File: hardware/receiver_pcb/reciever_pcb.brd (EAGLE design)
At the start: 54 x 27 mm, 26 parts

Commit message: better dir struct, and some tweaks to pcbs
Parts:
- removed R6: 220, rcl:R0805
- removed T1: (no value), transistor:SOT23-BCE
- added LED2: (no value), led:CHIP-LED0805
- R4, R5: value 10K -> 470
- moved R5 10.4 mm to (32.4, 21.9), turned to 90 degrees
- moved TP2 10.1 mm to (36.1, 18.6)
- moved R4 9.09 mm to (30.0, 22.0), turned to 90 degrees
- moved LED1 2.26 mm to (32.4, 18.1), turned to 180 degrees
- moved X1 1.00 mm to (43.8, 23.0)
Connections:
- removed net N$12: R6.2, T1.C, X3.3
- new net N$13: LED2.C, TP1.TP, U$1.P$15
- net +4.1V: now also R4.2, R5.2; no longer T1.E
- net GND: no longer LED1.C
- net N$10: now also LED2.A; no longer TP1.TP, U$1.P$15
- net N$11: now also R5.1; no longer R6.1
- net N$9: now also LED1.C; no longer R5.1, T1.B
- net VCC: no longer R4.2, R5.2
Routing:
- net +4.1V: track 40.7 -> 78.3 mm
- net N$9: track 33.3 -> 8.84 mm
- net N$12: track 14.0 -> 0.00 mm, vias 1 -> 0
- net GND: track 42.8 -> 30.7 mm, vias 2 -> 0
- net N$10: track 12.9 -> 2.00 mm
- net N$13: track 0.00 -> 8.68 mm
- net VCC: track 42.1 -> 35.6 mm
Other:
- outline, holes or cut-outs redrawn

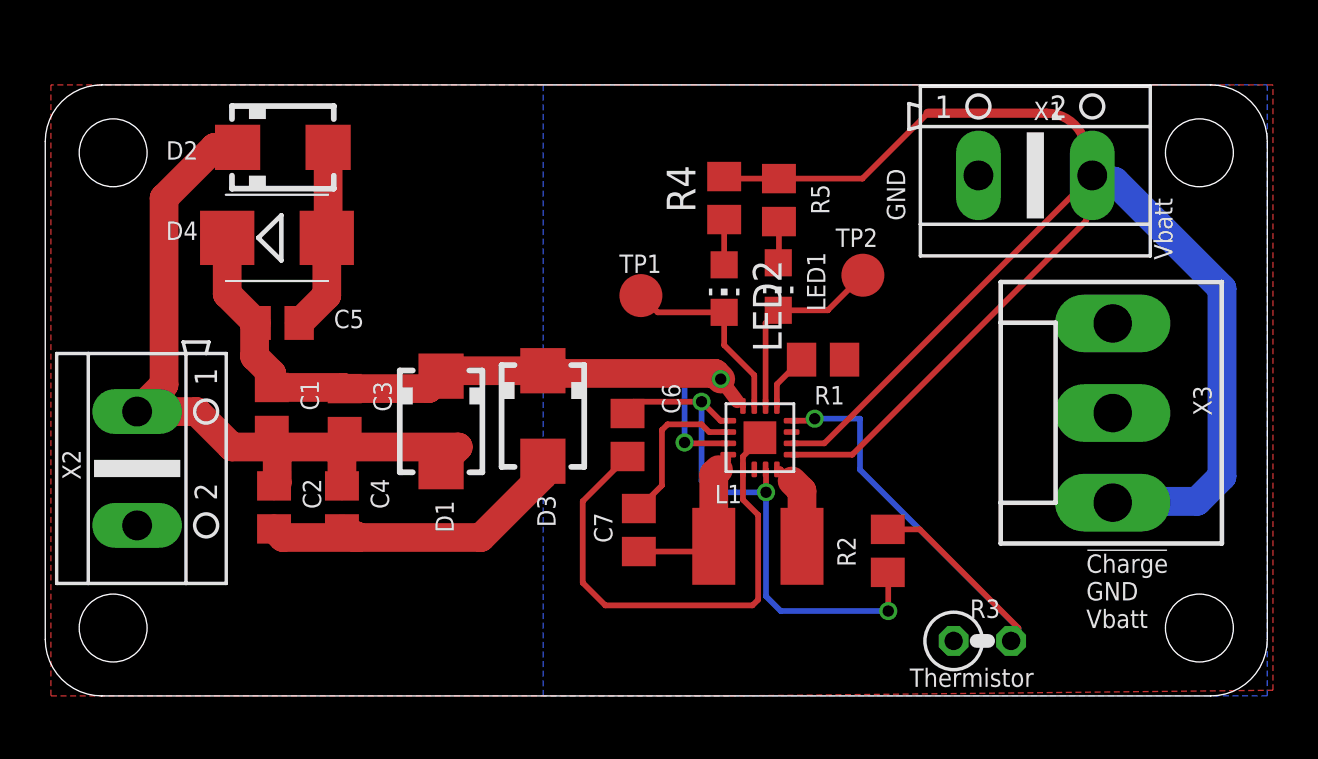
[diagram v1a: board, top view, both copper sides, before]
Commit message: checkpoints revised with Matt, new footprints
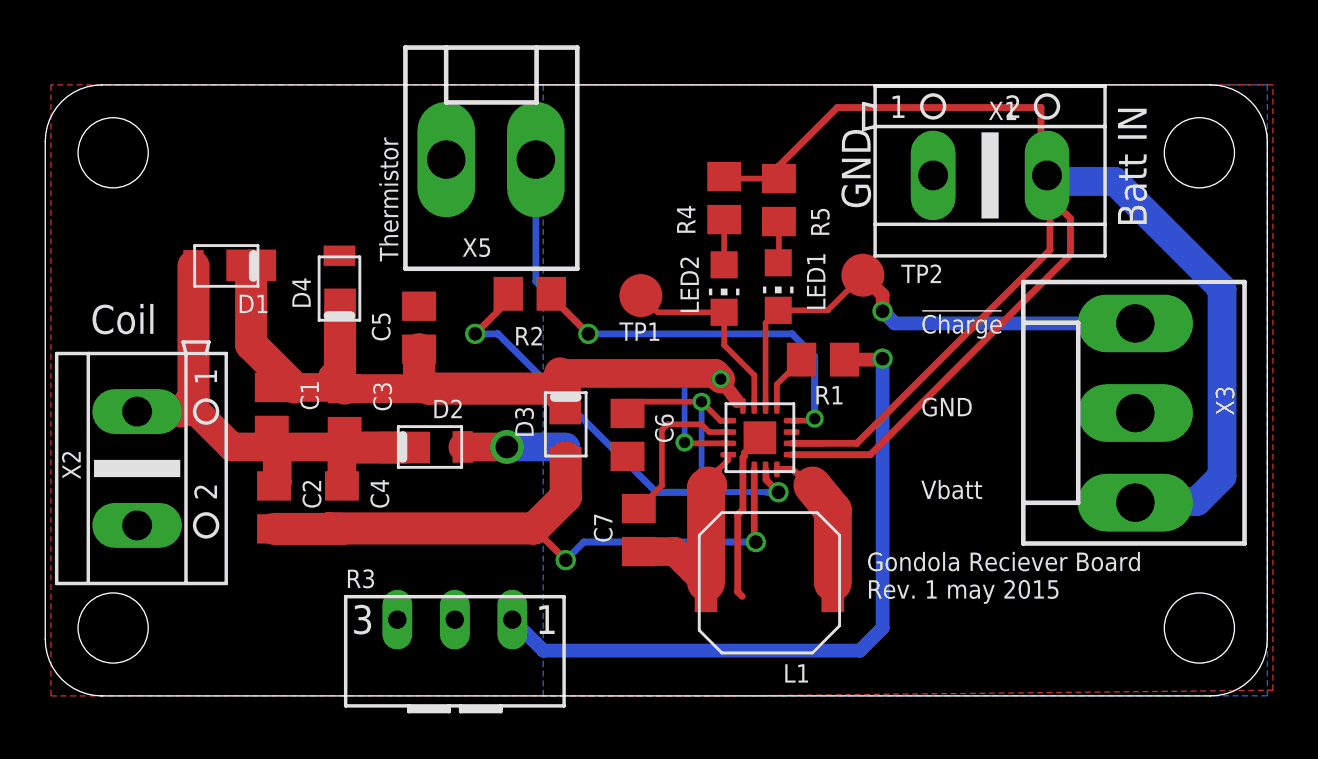
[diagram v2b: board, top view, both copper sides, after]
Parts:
- added X5: (no value), con-molex:KK-156-2
- D1, D2, D3: value 40V 2A -> DFLS240L; device diode:SMA -> custom parts:POWERDI123
- D4: value 39V -> 39VZ; device diode:SMB -> custom parts:POWERDI123
- L1: device rcl:L1812 -> custom parts:D62LCB
- R3: value thermistor -> 22K; device rcl:0207/2V -> pot:S63S
- moved R3 23.3 mm to (18.1, 2.10)
- moved R2 19.5 mm to (21.4, 17.8), turned to 180 degrees
- moved D2 14.7 mm to (17.0, 11.0)
- moved D1 11.7 mm to (8.00, 19.0), turned to 180 degrees
- moved C5 6.25 mm to (16.5, 16.3), turned to 90 degrees
- moved D4 3.55 mm to (13.0, 18.0), turned to 90 degrees
- moved X1 2.00 mm to (41.8, 23.0)
- moved L1 1.69 mm to (32.0, 5.00), turned to 180 degrees
- moved D3 1.08 mm to (23.0, 12.0)
- moved X3 1.00 mm to (48.2, 12.5)
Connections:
- new net N$12: R1.2, R3.A
- net GND: now also R3.E, R3.S, X5.1; no longer R1.2, R3.1
- net N$1: now also D2.K; no longer D2.C
- net N$2: now also U$1.P$6
- net N$5: now also L1.P$2; no longer L1.1
- net N$6: now also L1.P$1; no longer L1.2
- net N$8: now also X5.2; no longer R3.2
- net N$9: now also X3.3
- net VCC: now also D1.K, D3.K, D4.K; no longer D1.C, D3.C, D4.C
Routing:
- net N$12: track 0.00 -> 30.9 mm, vias 0 -> 1
- net GND: track 30.7 -> 12.0 mm, vias 0 -> 1
- net N$2: track 14.6 -> 29.8 mm, vias 0 -> 2
- net N$9: track 8.84 -> 22.2 mm, vias 0 -> 1
- net N$1: track 35.2 -> 24.2 mm
- net +4.1V: track 78.3 -> 84.3 mm
- net VCC: track 35.6 -> 40.9 mm
- net N$3: track 24.7 -> 28.9 mm
- net N$8: track 24.2 -> 27.2 mm, vias 1 -> 2
- net N$6: track 3.95 -> 6.44 mm
- net N$5: track 7.72 -> 9.61 mm
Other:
- board text added: "Batt IN"
- board text added: "Coil"
- board text added: "Gondola Reciever Board Rev. 1 may 2015"
- board text removed: "Vbatt"

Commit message: last touches befor OSHP
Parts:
- moved R2 0.73 mm to (21.6, 17.1)
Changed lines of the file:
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@@
 <setting verticaltext="up"/>
 </settings>
-<grid distance="1" unitdist="mm" unit="mm" style="lines" multiple="1" display="no" altdistance="0.1" altunitdist="mm" altunit="mm"/>
+<grid distance="0.1" unitdist="mm" unit="mm" style="lines" multiple="1" display="no" altdistance="0.1" altunitdist="mm" altunit="mm"/>
 <layers>
 <layer number="1" name="Top" color="4" fill="1" visible="yes" active="yes"/>
@@
 <attribute name="VALUE" x="33.735" y="12.32" size="1.27" layer="27"/>
 </element>
-<element name="R2" library="rcl" package="R0805" value="10K" x="21.41" y="17.77" smashed="yes" rot="R180">
-<attribute name="NAME" x="22.045" y="16.3" size="0.8128" layer="25" rot="R180"/>
-<attribute name="VALUE" x="22.045" y="20.31" size="1.27" layer="27" rot="R180"/>
+<element name="R2" library="rcl" package="R0805" value="10K" x="21.61" y="17.07" smashed="yes" rot="R180">
+<attribute name="NAME" x="22.245" y="15.6" size="0.8128" layer="25" rot="R180"/>
+<attribute name="VALUE" x="22.245" y="19.61" size="1.27" layer="27" rot="R180"/>
 </element>
 <element name="R5" library="rcl" package="R0805" value="470" x="32.42" y="21.91" smashed="yes" rot="R90">
@@
 <wire x1="30.9" y1="10.73" x2="31.58" y2="11.41" width="0.3048" layer="1"/>
 <contactref element="X5" pad="1"/>
-<wire x1="30.83" y1="10.01" x2="30.83" y2="8.23" width="0.3048" layer="1"/>
 <wire x1="30.83" y1="8.23" x2="30.6" y2="8" width="0.3048" layer="1"/>
 <wire x1="30.6" y1="8" x2="30.6" y2="4.6" width="0.3048" layer="1"/>
 <wire x1="30.6" y1="4.6" x2="30.8" y2="4.4" width="0.3048" layer="1"/>
+<wire x1="30.83" y1="10.01" x2="30.83" y2="8.23" width="0.3048" layer="1"/>
 </signal>
 <signal name="N$1">
@@
 <wire x1="29" y1="13" x2="26" y2="13" width="0.254" layer="1"/>
 <wire x1="26" y1="13" x2="25.73" y2="12.48" width="0.254" layer="1"/>
-<wire x1="20.46" y1="17.77" x2="20.46" y2="17.46" width="0.3048" layer="1"/>
+<wire x1="20.66" y1="17.07" x2="20.46" y2="17.46" width="0.3048" layer="1"/>
 <wire x1="20.46" y1="17.46" x2="19" y2="16" width="0.3048" layer="1"/>
 <via x="19" y="16" extent="1-16" drill="0.6"/>
@@
 <wire x1="33.91" y1="12.16" x2="34" y2="12.25" width="0.254" layer="1"/>
 <via x="34" y="12.25" extent="1-16" drill="0.5"/>
-<wire x1="22.36" y1="17.77" x2="22.36" y2="17.64" width="0.3048" layer="1"/>
+<wire x1="22.56" y1="17.07" x2="22.36" y2="17.64" width="0.3048" layer="1"/>
 <wire x1="22.36" y1="17.64" x2="24" y2="16" width="0.3048" layer="1"/>
 <via x="24" y="16" extent="1-16" drill="0.6"/>
